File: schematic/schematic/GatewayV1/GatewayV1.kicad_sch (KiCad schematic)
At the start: 33 parts, among them Q3 BC557, Q4 BC557, Q5 FDS9926A, SW1 SW_Push, SW2 SW_Push, U1 ESP-12E, U3 ADS1115IDGS, U4 TP4056-42-ESOP8, U5 DW01A

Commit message: Refactor: Updated ESP
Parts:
- removed C6, C7: 100nF, symbol Device:C
- removed D2, D3: LED, symbol Device:LED
- removed Q5: FDS9926A, Package_SO:SOIC-8_3.9x4.9mm_P1.27mm, symbol Transistor_FET:FDS9926A
- removed R6, R7: R10K, symbol Device:R
- removed R8: R2K, symbol Device:R
- removed U1: ESP-12E, RF_Module:ESP-12E, symbol RF_Module:ESP-12E
- removed U4: TP4056-42-ESOP8, Package_SO:SOIC-8-1EP_3.9x4.9mm_P1.27mm_EP2.41x3.3mm_ThermalVias, symbol Battery_Management:TP4056-42-ESOP8
- removed U5: DW01A, Package_TO_SOT_SMD:SOT-23-6, symbol Battery_Management:DW01A
- added Q5: BC557, Package_TO_SOT_THT:TO-92_Inline, symbol Transistor_BJT:BC557
- added R23: R10K, symbol Device:R
- added U4: 2.4GHz, easyEDA:WIFIM-SMD_ESP-12F-ESP8266MOD, symbol easyEDA:ESP-12F(ESP8266MOD)
- R18: value 1.2K -> 100K
- R19: value 1K -> 1M
- R20: value 1K -> 100K
- R21: value 100 -> R2K
- R22: value 1K -> R10K
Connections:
- net ENA_PEON_SOLAR is gone; now on net ENA_READ_VOLTAGE: R15.1
- net +3.3V: now also R22.1, R23.1
- net ADC_3: now also R19.2, R20.1
- net GND: now also R20.2; no longer R18.1, R22.2
- net SCL: now also U4.14 (GPIO5)
- net SDA: now also U4.13 (GPIO4)
- net RST: now reaches R21.2
- net RST: now also R22.2, SW2.2, U4.1 (RST)
- net ENA: now reaches SW1.2
- net ENA: now also R23.2, U4.3 (EN)
- net at R19.1: now also Q5.1 (C); no longer R20.1
- net at R18.2: now also Q5.2 (B)
- net BAT+: no longer names the net of R21.1
- net BAT+: now also U4.4 (GPIO16)
- net ENA_PEON_BAT renamed ENA_READ_VOLTAGE
- net ENA_READ_VOLTAGE: now also R18.1, U4.20 (GPIO10)
- new net BAT: Q5.3 (E)
- new net PEON_PULSE: U4.5 (GPIO14)
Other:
- moved on the sheet: R10, R11, R9, SW1, SW2

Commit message: Feat: Updated components
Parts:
- removed SW1: SW_Push, symbol Switch:SW_Push
- R10, R9: value 10K -> 10kΩ; footprint (none) -> easyEDA:R1206; symbol Device:R -> easyEDA:1206W4F1002T5E; LCSC Part Name (none) -> 10kΩ ±1% 250mW 厚膜电阻; Manufacturer (none) -> UNI-ROYAL(厚声); Manufacturer Part (none) -> 1206W4F1002T5E; Supplier (none) -> LCSC; Supplier Part (none) -> C17902
- R11: value 10K -> 10kΩ; footprint (none) -> easyEDA:R1206; symbol Device:R -> easyEDA:1206W4F1002T5E; JLCPCB Part (none) -> C17902; LCSC Part Name (none) -> 10kΩ ±1% 250mW 厚膜电阻; MFR.Part  (none) -> 1206W4F1002T5E; Manufacturer (none) -> UNI-ROYAL(厚声); Manufacturer Part (none) -> 1206W4F1002T5E; Precio (none) -> 0.01; Supplier (none) -> LCSC; Supplier Part (none) -> C17902
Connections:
- net +3.3V: now also R10.2, R11.2, R9.2; no longer R10.1, R11.1, R9.1
- net ADC_ALERT: now also R10.1; no longer R9.2
- net SCL: now also R9.1; no longer R10.2
- net SDA: now also R11.1; no longer R11.2

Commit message: Feat: Updated components
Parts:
- removed 10K: R, symbol Device:R
- removed C4: 0.1uF, symbol Device:C
- removed Q3, Q4, Q5: BC557, Package_TO_SOT_THT:TO-92_Inline, symbol Transistor_BJT:BC557
- removed R12, R16, R19: 1M, symbol Device:R
- removed R13, R14, R15, R17, R18, R20: 100K, symbol Device:R
- removed R21: R2K, symbol Device:R
- removed R22, R23: R10K, symbol Device:R
- removed U3: ADS1115IDGS, Package_SO:TSSOP-10_3x3mm_P0.5mm, symbol Analog_ADC:ADS1115IDGS
- added C6, C7: 100nF, easyEDA:C1206, symbol easyEDA:CC1206KRX7R9BB104
- added Q5, Q6, Q7: ~, easyEDA:SOT-23-3_L2.9-W1.3-P1.90-LS2.4-BR, symbol easyEDA:MMBT5401_C7420356
- added R15, R16, R19, R22, R24, R6, R7, R8: 1kΩ, easyEDA:R1206, symbol easyEDA:1206W4F1001T5E
- added R18, R20, R21, R23, R25, R27, R28, R29, R30, R31: 10kΩ, easyEDA:R1206, symbol easyEDA:1206W4F1002T5E
- added R26: R10K, symbol Device:R
- added U1: ~, easyEDA:SC-70-5_L2.1-W1.3-P0.65-LS2.1-BR, symbol easyEDA:SN74LVC1G08DCKR
- added U5: ~, easyEDA:SOT-23-5_L3.0-W1.7-P0.95-LS2.8-BR, symbol easyEDA:SN74LVC1G32DBVR
- added U6: ~, easyEDA:MSOP-10_L3.0-W3.0-P0.50-LS5.0-BL, symbol easyEDA:ADS1115IDGSR
- C5: footprint (none) -> easyEDA:C1206; symbol Device:C -> easyEDA:CL31B105KBHNNNE; LCSC Part Name (none) -> 1uF ±10% 50V; Manufacturer (none) -> SAMSUNG(三星); Manufacturer Part (none) -> CL31B105KBHNNNE; Supplier (none) -> LCSC; Supplier Part (none) -> C1848
- SW2: footprint (none) -> easyEDA:SW-SMD_L3.9-W3.0-P4.45; symbol Switch:SW_Push -> easyEDA:TS-1088-AR02016; LCSC Part Name (none) -> 4*3*2mm 立贴 轻触开关; Manufacturer (none) -> XUNPU(讯普); Manufacturer Part (none) -> TS-1088-AR02016; Supplier (none) -> LCSC; Supplier Part (none) -> C720477
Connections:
- net +3.3V: now also U4.8 (VCC), R21.2, R25.2, R26.2, R27.2, R28.2, R29.2, R30.2, U1.5 (VCC), U5.5 (VCC)
- net +5V: now also C5.2, C7.2, U6.8 (VDD); no longer C5.1
- net ADC_0: now also U6.4 (AIN0)
- net ADC_1: now also R23.1, R24.2, U6.5 (AIN1)
- net ADC_2: now also R20.1, R22.2, U6.6 (AIN2)
- net ADC_3: now also R18.1, R19.2, U6.7 (AIN3)
- net ADC_ALERT: now also U6.2 (ALERT/RDY)
- net BAT: now also Q5.2 (E)
- net ENA: now also R29.1
- net ENA_READ_VOLTAGE: now also R15.1, R16.1, R8.1
- net GND: now also C5.1, C6.1, C7.1, R19.1, R22.1, R24.1, R31.2, U1.3 (GND), U5.3 (GND), U6.3 (GND); no longer C5.2
- net PEON_BAT: now also Q7.2 (E)
- net PEON_SOLAR: now also Q6.2 (E)
- net RST: now also U4.7 (GPIO13), R21.1, U1.2 (B); no longer U4.1 (RST)
- net SCL: now also U6.10 (SCL)
- net SDA: now also U6.9 (SDA)
- net PROGRAM: now reaches U4.12 (GPIO0)
- net PROGRAM: now also R27.1
- net at U4.18 (MISO): now also R26.1
- net at U4.4 (GPIO16): now also R6.2
- net DRST: now reaches U4.6 (GPIO12)
- net DRST: now also R7.1
- new net: C6.2, R25.1, R7.2, U5.2 (B)
- new net: Q6.1 (B), R15.2
- new net: Q6.3 (C), R20.2
- new net: Q7.1 (B), R16.2
- new net: U1.4 (Y), U5.1 (A)
- new net: R31.1, U6.1 (ADDR)
- new net: Q5.1 (B), R8.2
- new net: Q5.3 (C), R18.2
- new net: Q7.3 (C), R23.2
- new net REBOOT: R28.1, U4.1 (RST), U5.4 (Y)
- new net WKP: R30.1, R6.1, U1.1 (A)
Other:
- note added: "Input RST = RESET WKP = WAKE UP DRST = DISABLE RESET RST | WKP | DRST | OUT X | X | 1 | 1 0 | X | 0 | 0 X | 0 | 0 | 1 OUT = (RST.WKP) + DRST GATES ARE SMITH TRIGGER"
- note added: "Para evitar glitches on boot esp"
- note added: "WARNING: ESP8266 algunos modelos tiene problema que se congela en boot después de un deep sleep. Por lo cual se ha agregado una resistencia en seria a la salida del pin WKP, y una resistencia PULL-UP en miso, que nos ayudará abarcar más varieda de placas. No obstante, se recomiendan las siguiente placas según prioridad. 1) 12-F de AI THINTER. (original) 2) 12-F ModelVendor 3) 12-F AZ-Delivery"

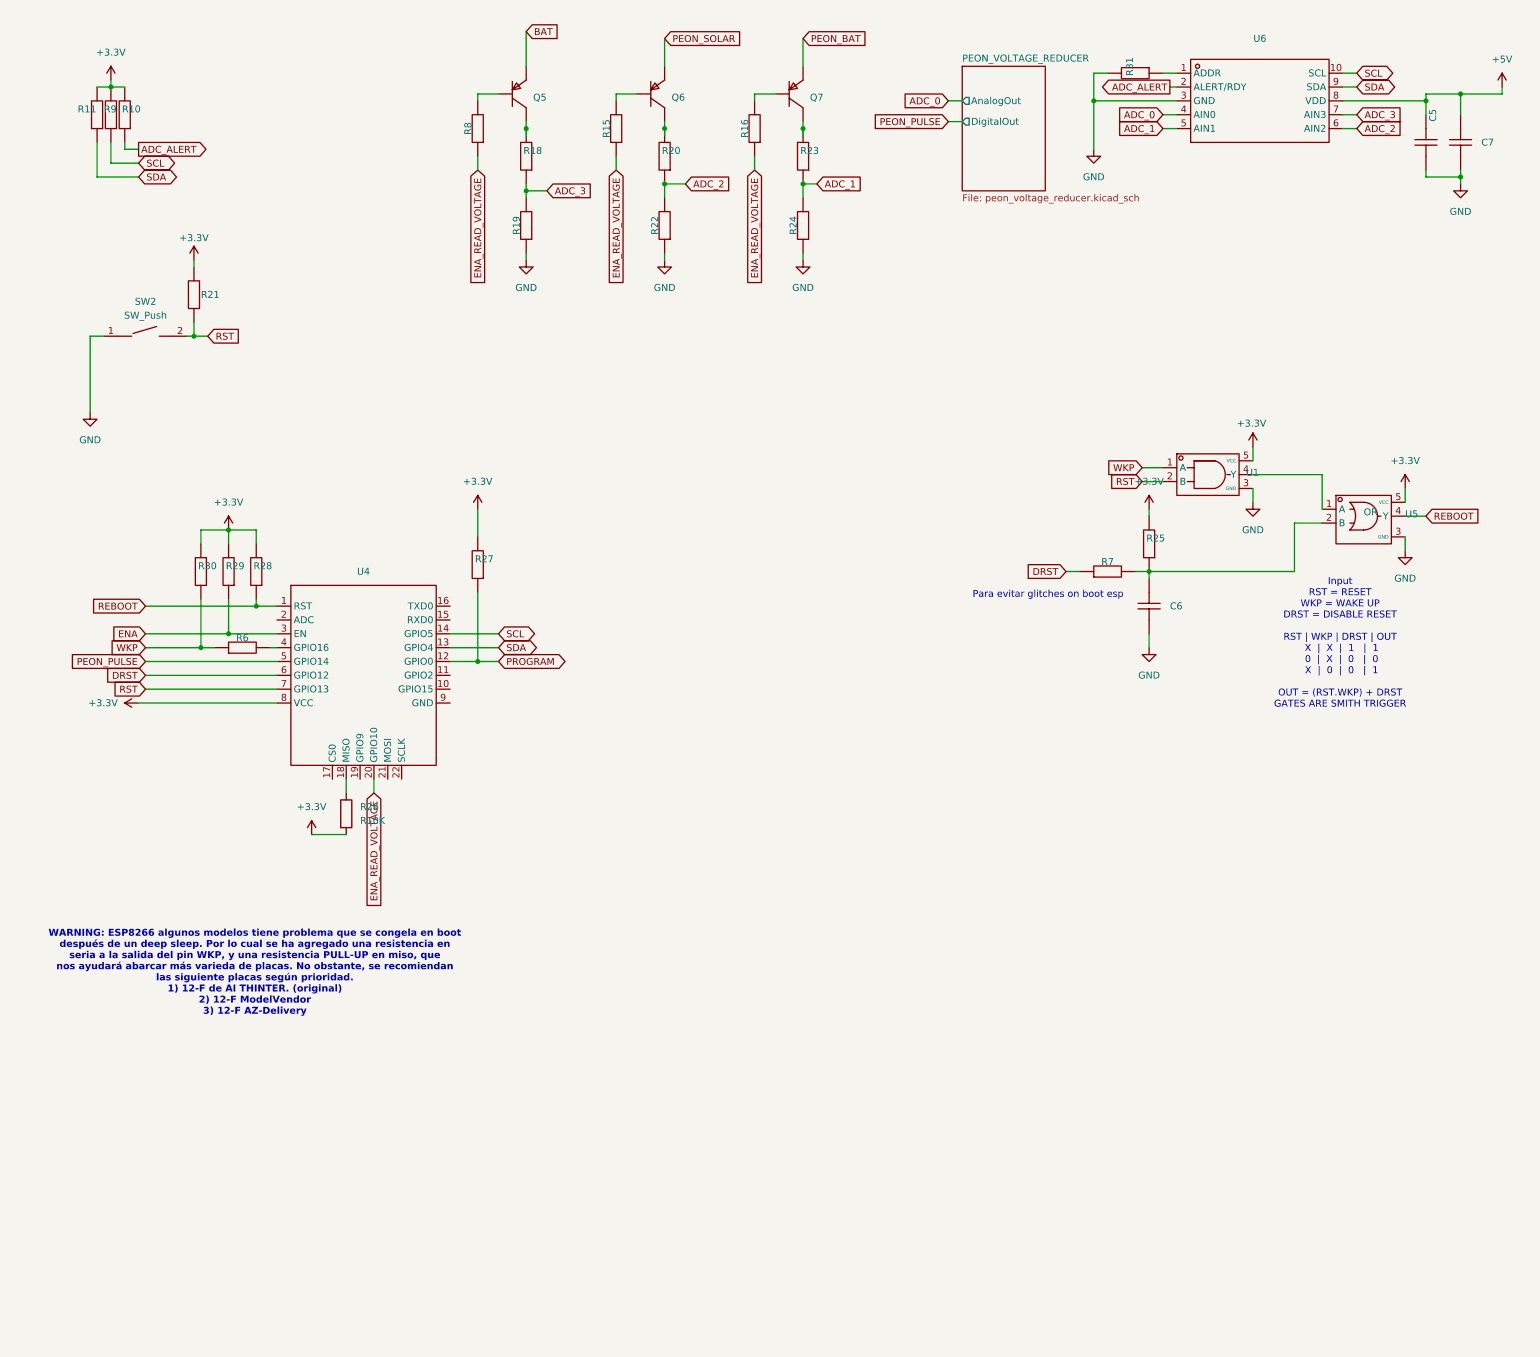
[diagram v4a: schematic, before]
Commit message: Feat: Added Lora
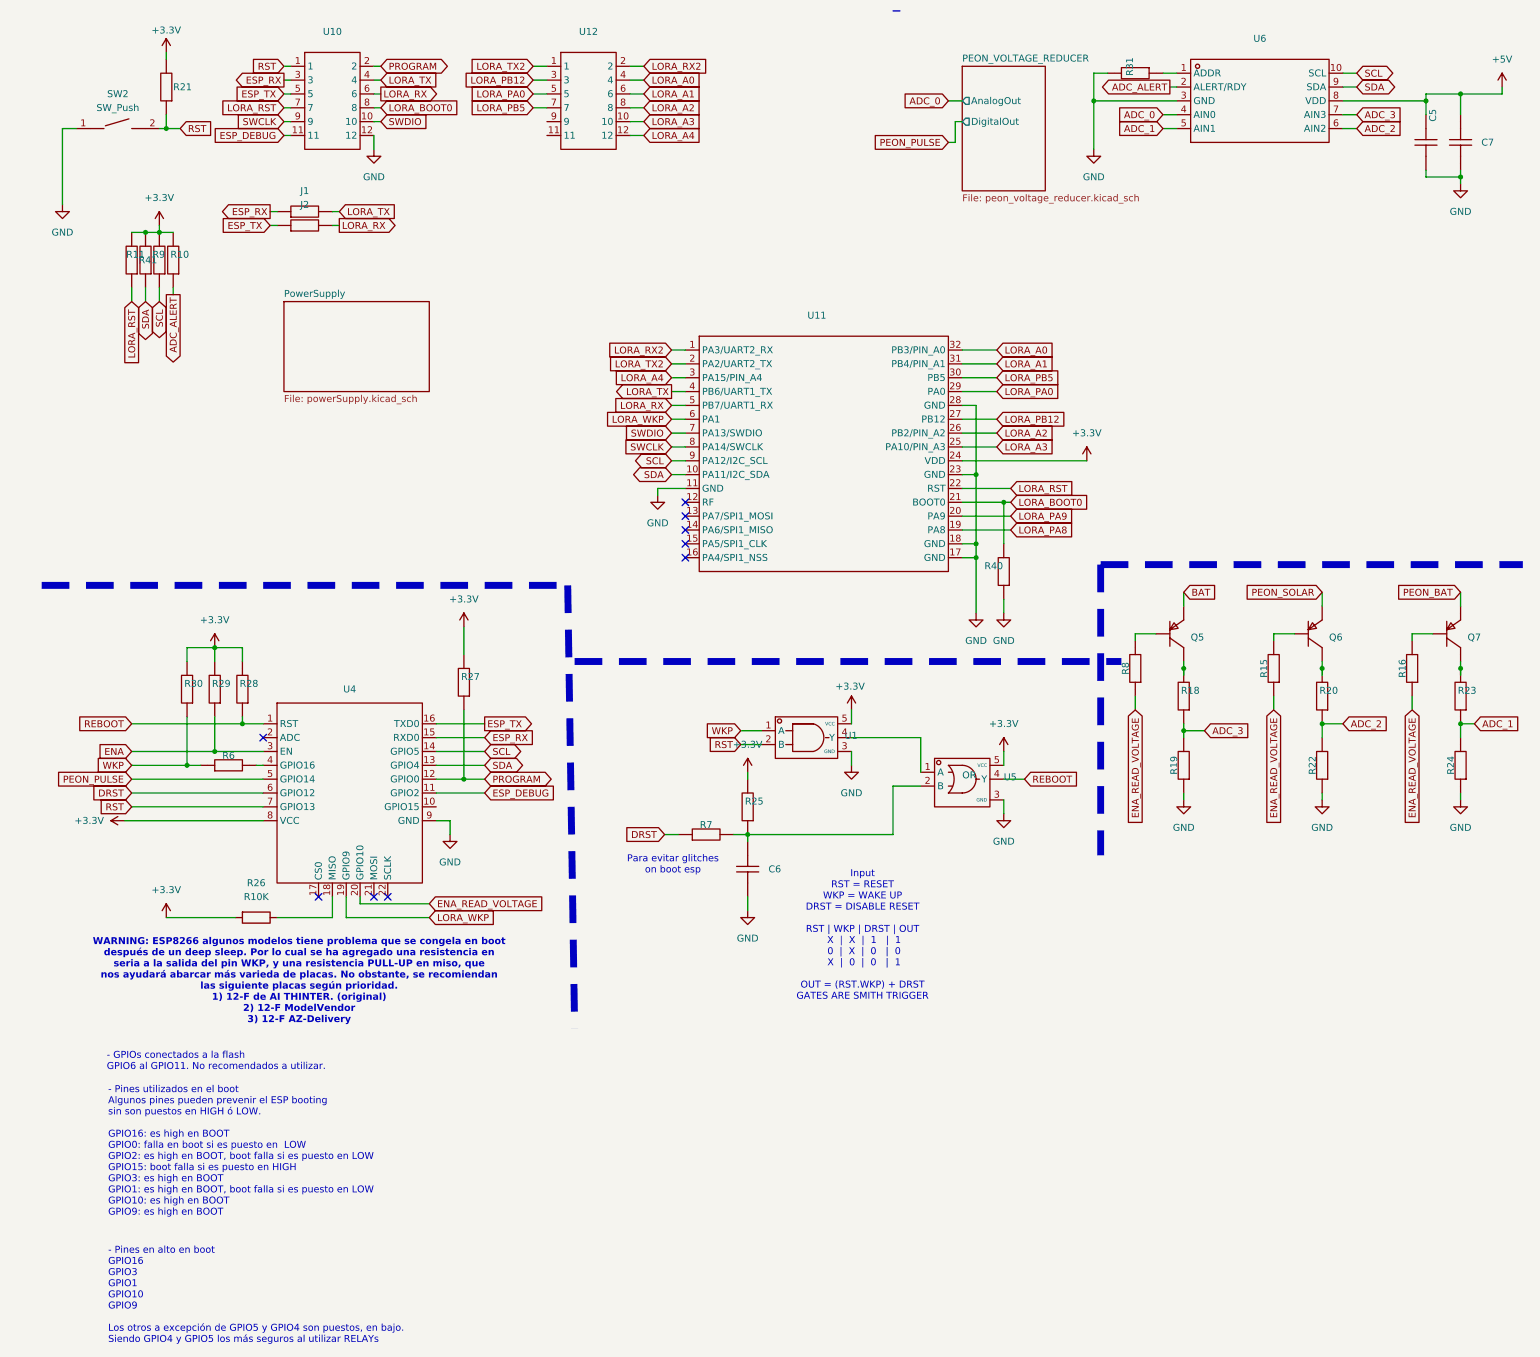
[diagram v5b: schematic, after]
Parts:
- added J1, J2: 0Ω, easyEDA:R0603, symbol easyEDA:0603WAJ0000T5E
- added R40, R41: 10kΩ, easyEDA:R1206, symbol easyEDA:1206W4F1002T5E
- added U10, U12: ~, easyEDA:HDR-TH_12P-P2.54-V-M-R2-C6-S2.54, symbol easyEDA:ZX-PZ2.54-2-6PZZ
- added U11: ~, easyEDA:WIRELM-SMD_32P-L15.5-W15.0-P1.00, symbol easyEDA:RAK3172-9-SM-I
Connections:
- net +3.3V: now also R41.2, U11.24 (VDD)
- net GND: now also U4.9 (GND), R40.1, U10.12, U11.11 (GND), U11.17 (GND), U11.18 (GND), U11.23 (GND), U11.28 (GND)
- net PROGRAM: now also U10.2
- net RST: now also U10.1
- net SCL: now also U11.9 (PA12/I2C_SCL)
- net SDA: now also U11.10 (PA11/I2C_SDA)
- net ESP_DEBUG: now reaches U4.11 (GPIO2)
- net ESP_DEBUG: now also U10.11
- net ESP_RX: now reaches U4.15 (RXD0)
- net ESP_RX: now also J1.1, U10.3
- net ESP_TX: now reaches U4.16 (TXD0)
- net ESP_TX: now also J2.1, U10.5
- net LORA_WKP: now reaches U4.19 (GPIO9)
- net LORA_WKP: now also U11.6 (PA1)
- new net LORA_A0: U11.32 (PB3/PIN_A0), U12.4
- new net LORA_A1: U11.31 (PB4/PIN_A1), U12.6
- new net LORA_A2: U11.26 (PB2/PIN_A2), U12.8
- new net LORA_A3: U11.25 (PA10/PIN_A3), U12.10
- new net LORA_A4: U11.3 (PA15/PIN_A4), U12.12
- new net LORA_BOOT0: R40.2, U10.8, U11.21 (BOOT0)
- new net LORA_PA0: U11.29 (PA0), U12.5
- new net LORA_PA8: U11.19 (PA8)
- new net LORA_PA9: U11.20 (PA9)
- new net LORA_PB12: U11.27 (PB12), U12.3
- new net LORA_PB5: U11.30 (PB5), U12.7
- new net LORA_RST: R41.1, U10.7, U11.22 (RST)
- new net LORA_RX: J2.2, U10.6, U11.5 (PB7/UART1_RX)
- new net LORA_RX2: U11.1 (PA3/UART2_RX), U12.2
- new net LORA_TX: J1.2, U10.4, U11.4 (PB6/UART1_TX)
- new net LORA_TX2: U11.2 (PA2/UART2_TX), U12.1
- new net SWCLK: U10.9, U11.8 (PA14/SWCLK)
- new net SWDIO: U10.10, U11.7 (PA13/SWDIO)
- no-connect marks 0 -> 9
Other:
- added sheet PowerSupply (powerSupply.kicad_sch)
- note added: "- GPIOs conectados a la flash GPIO6 al GPIO11. No recomendados a utilizar."
- note added: "- Pines en alto en boot GPIO16 GPIO3 GPIO1 GPIO10 GPIO9 Los otros a excepción de GPIO5 y GPIO4 son puestos, en bajo. Siendo GPIO4 y GPIO5 los más seguros al utilizar RELAYs"
- note added: "- Pines utilizados en el boot Algunos pines pueden prevenir el ESP booting sin son puestos en HIGH ó LOW. GPIO16: es high en BOOT GPIO0: falla en boot si es puesto en LOW GPIO2: es high en BOOT, boot falla si es puesto en LOW GPIO15: boot falla si es puesto en HIGH GPIO3: es high en BOOT GPIO1: es high en BOOT, boot falla si es puesto en LOW GPIO10: es high en BOOT GPIO9: es high en BOOT"
- moved on the sheet: C6, Q5, Q6, Q7, R10, R11, R15, R16, R18, R19, R20, R21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

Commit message: Feat: Working in PCB files
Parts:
- removed R26: R10K, symbol Device:R
- added C18, C20, C22: 1uF, easyEDA:C1206, symbol easyEDA:CL31B105KBHNNNE
- added C19, C21, C23: 100nF, easyEDA:C1206, symbol easyEDA:CC1206KRX7R9BB104
- added P2: ~, easyEDA:CONN-TH_6P-P5.00_WJ126V-5.0-6P, symbol easyEDA:WJ126V-5.0-6P
- added R10: 10kΩ, easyEDA:R1206, symbol easyEDA:1206W4F1002T5E
- added R43: 220Ω, easyEDA:R1206, symbol easyEDA:1206W4F2200T5E
- added U13: ~, easyEDA:LED0603-RD, symbol easyEDA:F.0603.00139/P2-0603R1TS2-06T-002
- renumbered C6 to C1, C5 to C2, C7 to C3, Q5 to Q1, Q6 to Q2, Q7 to Q3, R41 to R1, R27 to R11, R7 to R12, R25 to R13, R40 to R14, R31 to R15, R8 to R16, R18 to R17, R19 to R18, R15 to R19, R11 to R2, R22 to R21, R16 to R22, R9 to R3, R21 to R4, R10 to R5, R30 to R6, R29 to R7, R6 to R8, R28 to R9, SW2 to SW1, U10 to U1, U4 to U2, U12 to U3, U1 to U4, U11 to U5, U5 to U6, U6 to U7
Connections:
- net +3.3V: now also C18.2, C19.2, C20.2, C21.2, C22.2, C23.2, R10.2
- net ADC_0: now also R17.1, R18.2
- net ADC_3: no longer R17.1, R18.2
- net BAT: now also P2.1
- net ESP_DEBUG: now also U1.7; no longer U1.11
- net ESP_RX: now also U1.1; no longer U1.3
- net ESP_TX: now also U1.3; no longer U1.5
- net GND: now also U1.9, C18.1, C19.1, C20.1, C21.1, C22.1, C23.1, P2.2, P2.4, P2.6, U13.1 (K); no longer U1.12
- net LORA_A0: now also U3.3; no longer U3.4
- net LORA_A1: now also U3.5; no longer U3.6
- net LORA_A2: now also U3.12; no longer U3.8
- net LORA_A4: now also U3.4; no longer U3.12
- net LORA_BOOT0: now also U1.12; no longer U1.8
- net LORA_PA0: now also U3.9; no longer U3.5
- net LORA_PA8: now also U3.6
- net LORA_PA9: now also U3.8
- net LORA_PB12: now also U3.11; no longer U3.3
- net LORA_RST: now also U1.11; no longer U1.7
- net LORA_RX: now also U1.4; no longer U1.6
- net LORA_RX2: now also U3.1; no longer U3.2
- net LORA_TX: now also U1.2; no longer U1.4
- net LORA_TX2: now also U3.2; no longer U3.1
- net PEON_BAT: now also P2.3
- net PEON_SOLAR: now also P2.5
- net PROGRAM: now also U1.5; no longer U1.2
- net RST: now also U1.6; no longer U1.1
- net SWCLK: now also U1.10; no longer U1.9
- net SWDIO: now also U1.8; no longer U1.10
- net at U2.10 (GPIO15): now also R43.1
- net at U2.18 (MISO): now also R10.1
- new net: R43.2, U13.2 (A)
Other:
- moved on the sheet: R17

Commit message: Feat Board Completed, in production
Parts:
- added H1, H2, H3, H4, H5, H6: MountingHole, MountingHole:MountingHole_2.7mm_M2.5, symbol Mechanical:MountingHole
- C1, C19, C21, C23, C3: Comments (none) -> -; JLCPCB Part (none) -> C82601; LCSC (none) -> C82601
- C18, C2, C20, C22: Comments (none) -> -; JLCPCB Part (none) -> C1848; LCSC (none) -> C1848
- J1, J2: Comments (none) -> -; JLCPCB Part (none) -> C15402; LCSC (none) -> C15402
- P2: value ~ -> CONN-TH-6P-P5.00; Comments (none) -> -; JLCPCB Part (none) -> C8379; LCSC (none) -> C8379
- Q1, Q2, Q3: value ~ -> MMBT5401; JLCPCB Part (none) -> C7420356; LCSC (none) -> C7420356
- R1, R10, R11, R13, R15, R17, R20, R23, R3, R4, R5, R6, R7, R9: Comments (none) -> -; JLCPCB Part (none) -> C17902; LCSC (none) -> C17902
- R12, R16, R18, R19, R21, R22, R24, R8: Comments (none) -> -; JLCPCB Part (none) -> C4410; LCSC (none) -> C4410
- R14, R2: Comments (none) -> -; LCSC (none) -> C17902; MFR.Part  1206W4F1002T5E -> (none); Precio 0.01 -> (none)
- R43: JLCPCB Part (none) -> C17957; LCSC (none) -> C17957
- SW1: value SW_Push -> Btn; JLCPCB Part (none) -> C720477; LCSC (none) -> C720477
- U1, U3: value ~ -> Pin Header 2x6; JLCPCB Part (none) -> C7501277; LCSC (none) -> C7501277
- U13: value ~ -> Red LED; Comments (none) -> -; JLCPCB Part (none) -> C7496820; LCSC (none) -> C7496820
- U2: value 2.4GHz -> ESP8266MOD; JLCPCB Part (none) -> C82891; LCSC (none) -> C82891; Price 2.22 -> (none)
- U4: value ~ -> SN74LVC1G08DCKR; JLCPCB Part (none) -> C7832; LCSC (none) -> C7832; price 0.06 -> (none)
- U5: value ~ -> RAK3172-9; JLCPCB Part (none) -> C19723905; LCSC (none) -> C19723905
- U6: value ~ -> SN74LVC1G32DBVR; JLCPCB Part (none) -> C10096; LCSC (none) -> C10096; gate OR -> (none); price 0.06 -> (none)
- U7: value ~ -> ADS1115IDGSR; JLCPCB Part (none) -> C37593; LCSC (none) -> C37593

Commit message: Feat: Added comment for first board received
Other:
- note added: "Error de diseño en Fuente de 3.3v 1) No se esta activando la fuente, de momento se ha desoldado la R que va a tierra para forzar siempre enabled. Errores en el diseño en ESP, 1) J1 y J2, no deben ir en el BOM como componentes a soldar. 2) GPIO15, debe tener una resistencia de 10K a tierra, de lo contrario no funcionará. Para programar el ESP 1) Corregir los errores de diseño 2) Cortocircuitar C1,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"
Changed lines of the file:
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@@
+		)
+	)
+	(text "Error de diseño en Fuente de 3.3v\n1) No se esta activando la fuente, de momento se ha \ndesoldado la R que va a tierra para forzar siempre enabled.\n\nErrores en el diseño en ESP, \n1) J1 y J2, no deben ir en el BOM como componentes a soldar.\n2) GPIO15, debe tener una resistencia de 10K a tierra, de lo\ncontrario no funcionará.\n\nPara programar el ESP\n1) Corregir los errores de diseño\n2) Cortocircuitar C1, para que el botón RST funciona si no \ntiene el firmware correcto.\n"
+		(exclude_from_sim no)
+		(at 137.922 217.932 0)
+		(effects
+			(font
+				(size 1.27 1.27)
+				(thickness 0.254)
+				(bold yes)
+				(color 255 0 9 1)
+			)
+			(justify left)
 		)
 	)
